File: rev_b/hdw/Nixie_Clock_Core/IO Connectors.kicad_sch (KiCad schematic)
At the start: 4 parts

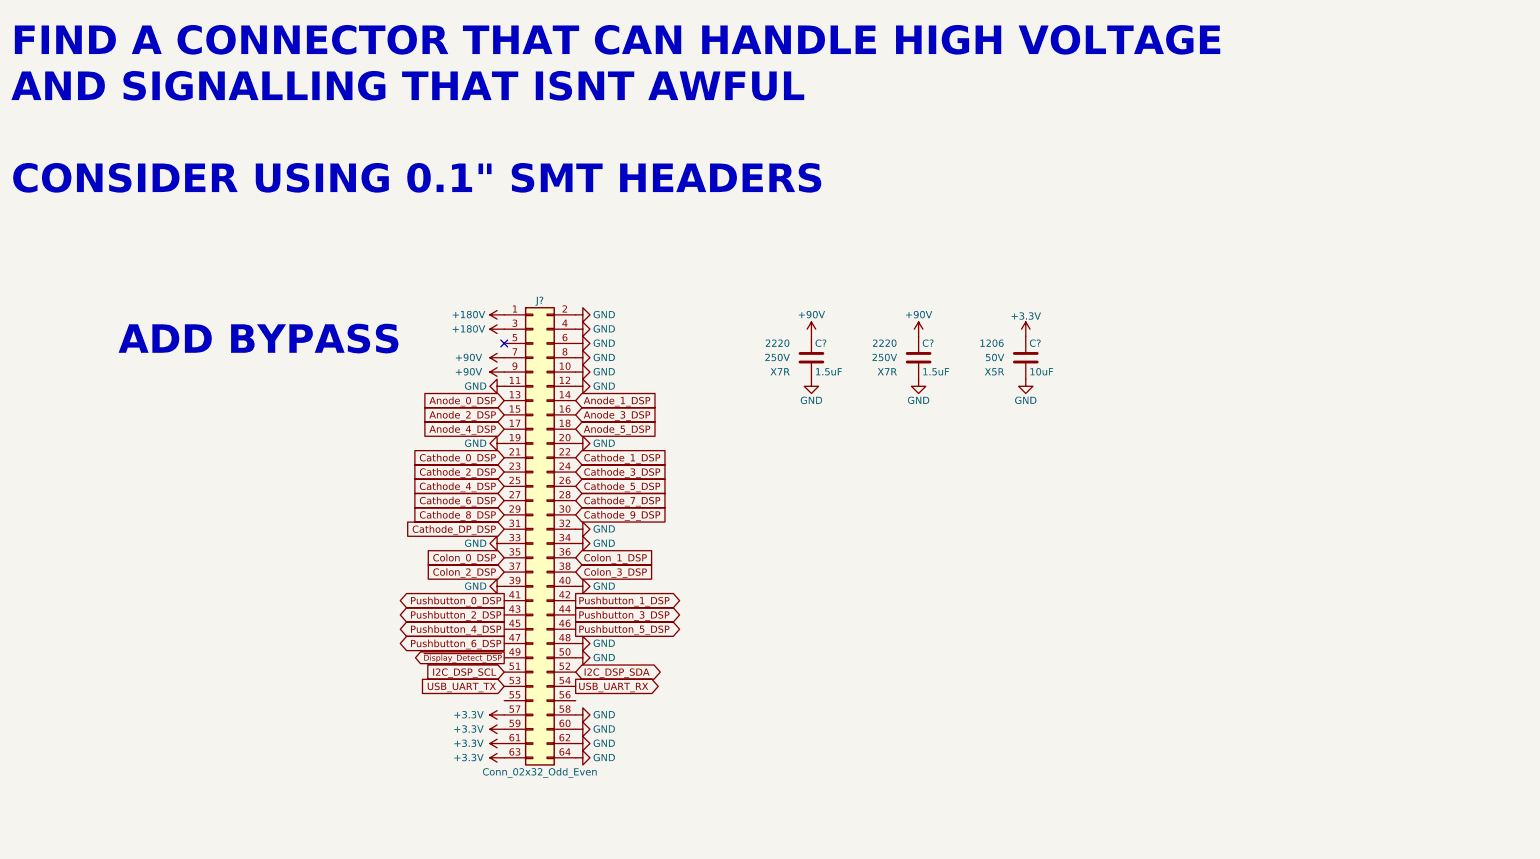
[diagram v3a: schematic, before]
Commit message: updated footprints, ran some DRC
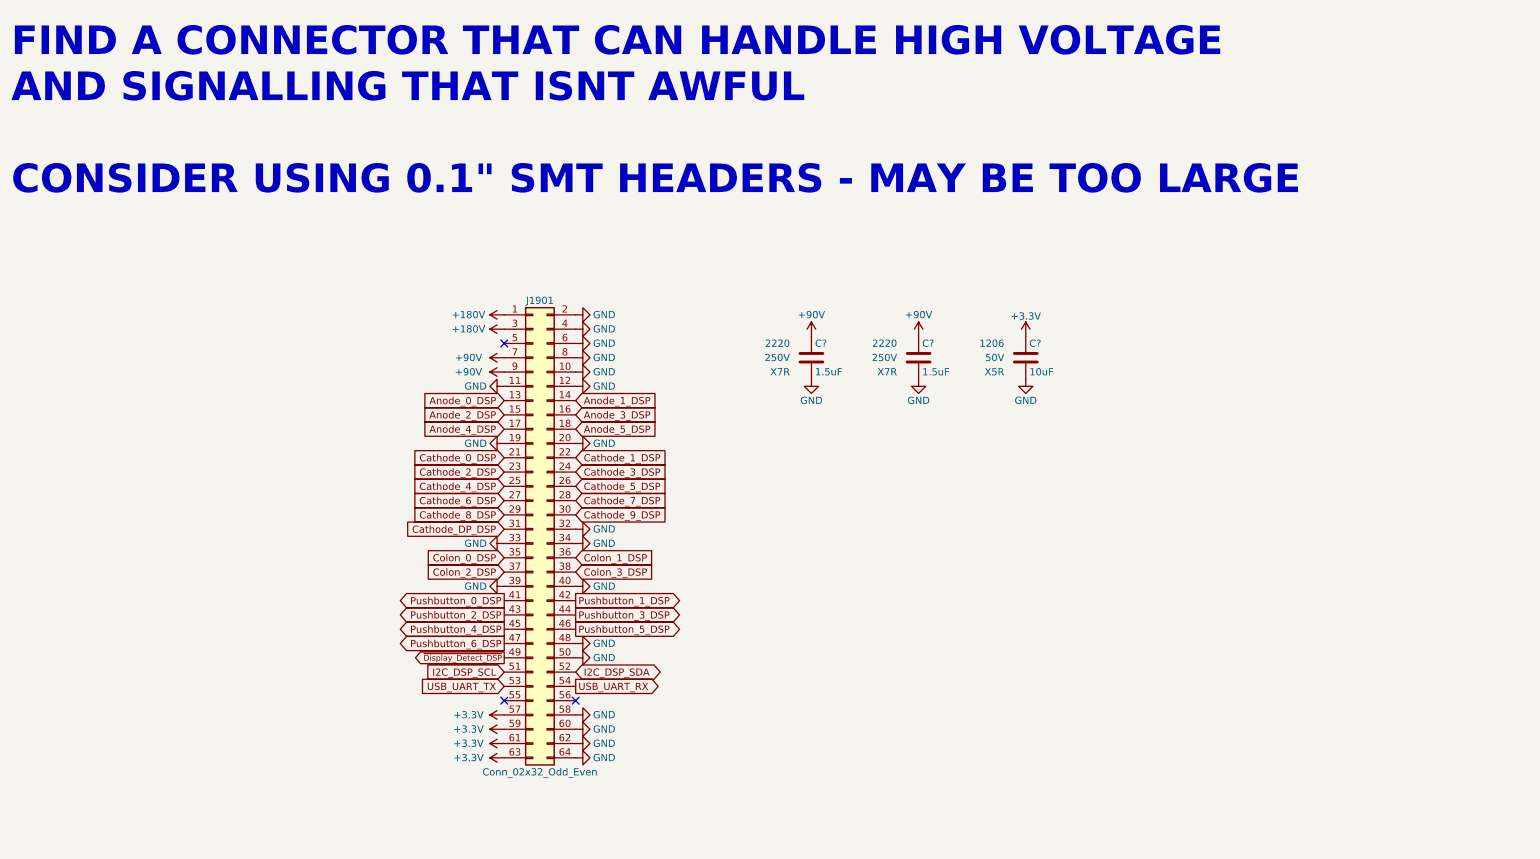
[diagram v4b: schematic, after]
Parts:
- C? (x2): footprint (none) -> Capacitors_SMD:C_2220; Digi-Key PN 565-4697-1-ND -> (none)
- C?: footprint (none) -> Capacitors_SMD:C_1206; Digi-Key PN 1276-6736-1-ND -> (none)
- J1901: renamed from J?; footprint (none) -> Connector_PinSocket_2.54mm:PinSocket_2x32_P2.54mm_Vertical_SMD
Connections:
- no-connect marks 1 -> 3
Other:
- note added: "FIND A CONNECTOR THAT CAN HANDLE HIGH VOLTAGE AND SIGNALLING THAT ISNT AWFUL CONSIDER USING 0.1" SMT HEADERS - MAY BE TOO LARGE"
- note removed: "ADD BYPASS"
- note removed: "FIND A CONNECTOR THAT CAN HANDLE HIGH VOLTAGE AND SIGNALLING THAT ISNT AWFUL CONSIDER USING 0.1" SMT HEADERS"
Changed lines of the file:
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@@
     (company "Drew Maatman")
   )
+  (no_connect (at 137.16 137.795))
+  (no_connect (at 124.46 137.795))
   (no_connect (at 124.46 74.295))
-  (text "ADD BYPASS" (at 55.88 76.835 0)
-    (effects (font (face "Courier New") (size 5.08 5.08) (thickness 0.254) bold (color 255 37 56 1)) (justify left bottom))
-  )
-  (text "FIND A CONNECTOR THAT CAN HANDLE HIGH VOLTAGE\nAND SIGNALLING THAT ISNT AWFUL\n\nCONSIDER USING 0.1\" SMT HEADERS"
+  (text "FIND A CONNECTOR THAT CAN HANDLE HIGH VOLTAGE\nAND SIGNALLING THAT ISNT AWFUL\n\nCONSIDER USING 0.1\" SMT HEADERS - MAY BE TOO LARGE"
     (at 36.83 48.26 0)
     (effects (font (face "Courier New") (size 5.08 5.08) (thickness 0.254) bold (color 255 37 56 1)) (justify left bottom))
@@
       (effects (font (size 1.27 1.27)) (justify left))
     )
-    (property "Footprint" "" (at 199.0852 80.645 0)
+    (property "Footprint" "Capacitors_SMD:C_2220" (at 199.0852 80.645 0)
       (effects (font (size 1.27 1.27)) hide)
     )
@@
       (effects (font (size 1.27 1.27)) (justify right))
     )
-    (property "Digi-Key PN" "565-4697-1-ND" (at 208.915 64.135 0)
+    (property "Digi-Key PN" "" (at 208.915 64.135 0)
       (effects (font (size 1.524 1.524)) hide)
     )
@@
         )
         (path "/16fdce21-b570-4d81-a458-e8839d611806/2e22fd27-425d-47fb-8810-3fe495af3afd"
-          (reference "C?") (unit 1)
+          (reference "C1902") (unit 1)
         )
       )
@@
       (effects (font (size 1.27 1.27)) (justify left))
     )
-    (property "Footprint" "" (at 218.1352 80.645 0)
+    (property "Footprint" "Capacitors_SMD:C_1206" (at 218.1352 80.645 0)
       (effects (font (size 1.27 1.27)) hide)
     )
@@
       (effects (font (size 1.27 1.27)) (justify right))
     )
-    (property "Digi-Key PN" "1276-6736-1-ND" (at 227.965 64.135 0)
+    (property "Digi-Key PN" "" (at 227.965 64.135 0)
       (effects (font (size 1.524 1.524)) hide)
     )
@@
         )
         (path "/16fdce21-b570-4d81-a458-e8839d611806/2e22fd27-425d-47fb-8810-3fe495af3afd"
-          (reference "C?") (unit 1)
+          (reference "C1903") (unit 1)
         )
       )
@@
   (symbol (lib_id "Connector_Generic:Conn_02x32_Odd_Even") (at 129.54 107.315 0) (unit 1)
     (in_bom yes) (on_board yes) (dnp no)
-    (property "Reference" "J?" (at 130.81 66.675 0)
+    (property "Reference" "J1901" (at 130.81 66.675 0)
       (effects (font (size 1.27 1.27)))
     )
@@
       (effects (font (size 1.27 1.27)))
     )
-    (property "Footprint" "" (at 129.54 107.315 0)
+    (property "Footprint" "Connector_PinSocket_2.54mm:PinSocket_2x32_P2.54mm_Vertical_SMD" (at 129.54 107.315 0)
       (effects (font (size 1.27 1.27)) hide)
     )
@@
       (project "Nixie_Clock_Core"
         (path "/16fdce21-b570-4d81-a458-e8839d611806/2e22fd27-425d-47fb-8810-3fe495af3afd"
-          (reference "J?") (unit 1)
+          (reference "J1901") (unit 1)
         )
       )
@@
       (effects (font (size 1.27 1.27)) (justify left))
     )
-    (property "Footprint" "" (at 180.0352 80.645 0)
+    (property "Footprint" "Capacitors_SMD:C_2220" (at 180.0352 80.645 0)
       (effects (font (size 1.27 1.27)) hide)
     )
@@
       (effects (font (size 1.27 1.27)) (justify right))
     )
-    (property "Digi-Key PN" "565-4697-1-ND" (at 189.865 64.135 0)
+    (property "Digi-Key PN" "" (at 189.865 64.135 0)
       (effects (font (size 1.524 1.524)) hide)
     )
@@
         )
         (path "/16fdce21-b570-4d81-a458-e8839d611806/2e22fd27-425d-47fb-8810-3fe495af3afd"
-          (reference "C?") (unit 1)
-        )
-      )
+          (reference "C1901") (unit 1)
+        )
+      )

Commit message: hid all passive refdes on core PCB
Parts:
- C?: Digi-Key PN (none) -> 1276-6767-1-ND
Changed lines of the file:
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@@
       (effects (font (size 1.27 1.27)) (justify right))
     )
-    (property "Digi-Key PN" "" (at 227.965 64.135 0)
+    (property "Digi-Key PN" "1276-6767-1-ND" (at 227.965 64.135 0)
       (effects (font (size 1.524 1.524)) hide)
     )

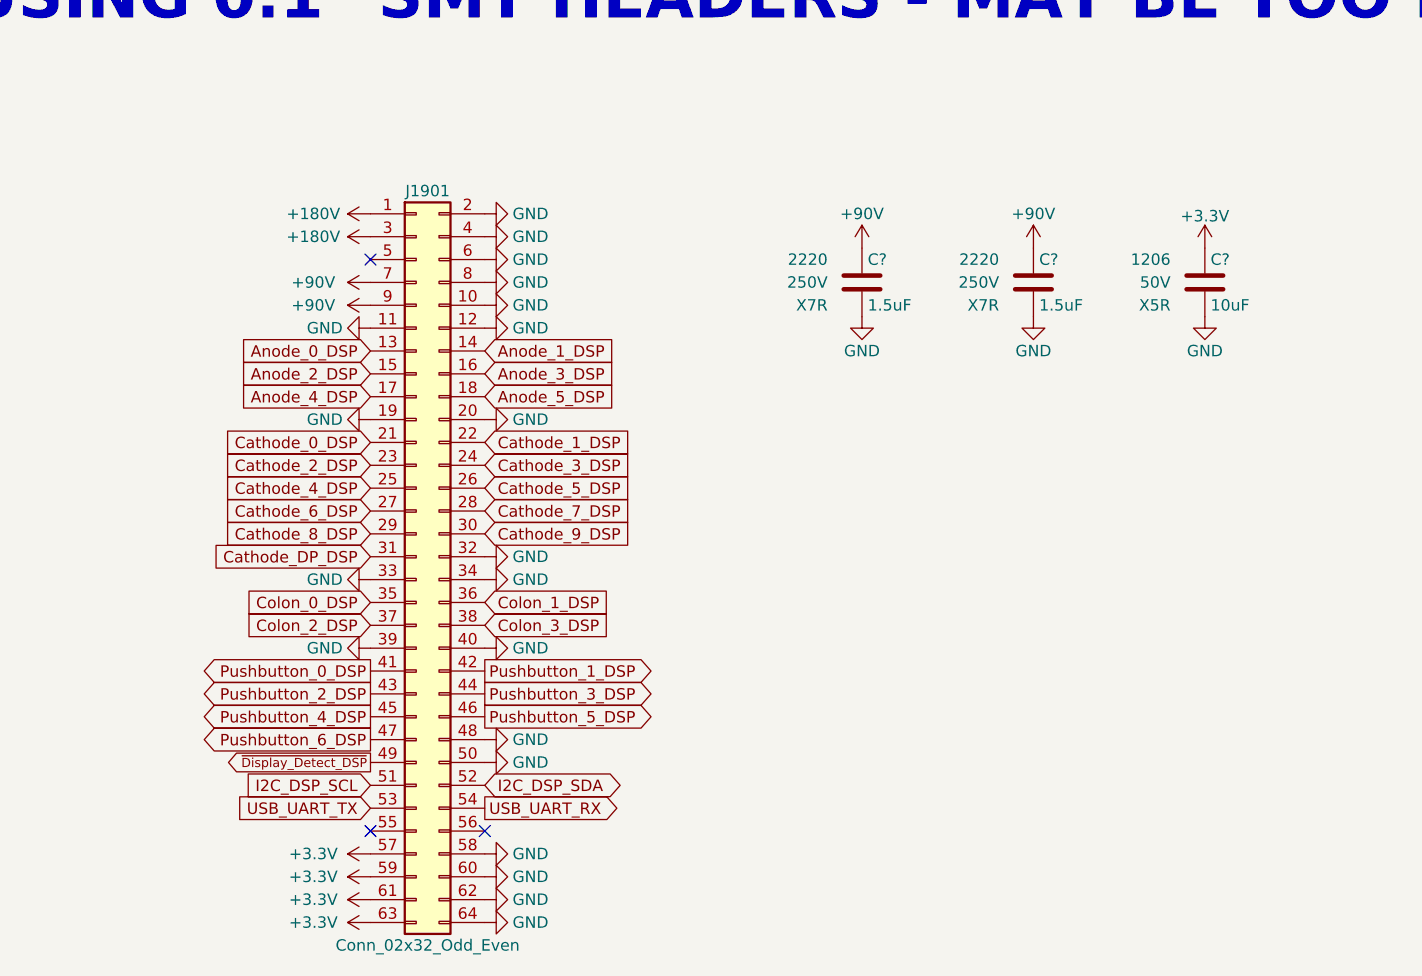
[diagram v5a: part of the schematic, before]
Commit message: chose new IO connector, fixed some net connectivity issues
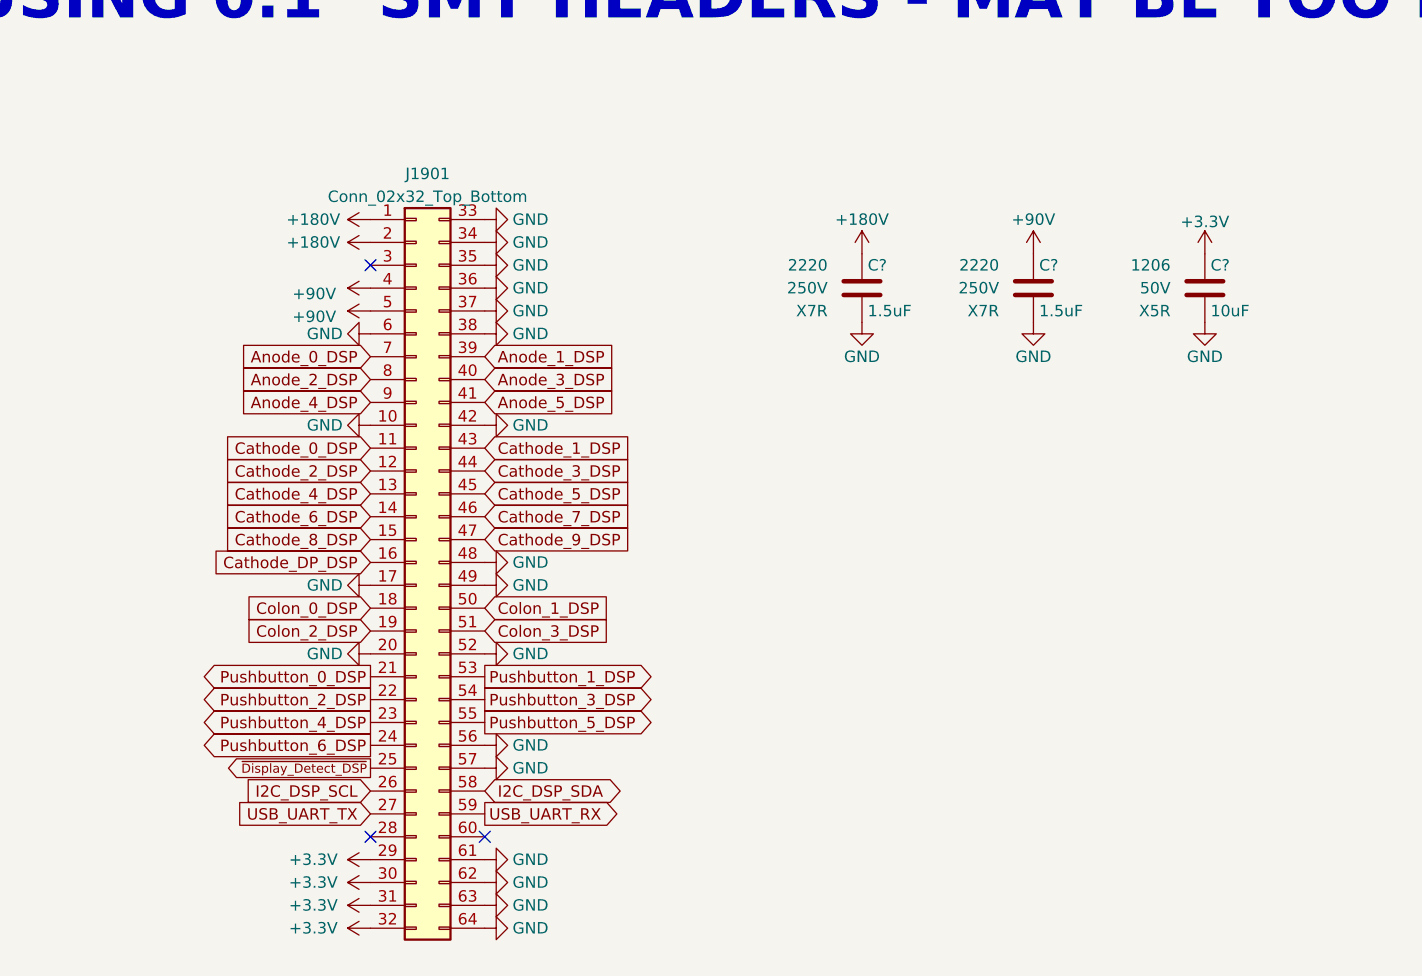
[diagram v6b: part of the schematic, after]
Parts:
- removed J1901: Conn_02x32_Odd_Even, Connector_PinSocket_2.54mm:PinSocket_2x32_P2.54mm_Vertical_SMD, symbol Connector_Generic:Conn_02x32_Odd_Even
- added J1901: Conn_02x32_Top_Bottom, Custom Footprints Library:CONN_5120527-1_TYC, symbol Connector_Generic:Conn_02x32_Top_Bottom
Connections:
- net +180V: now also C?.1, J1901.1 (Pin_1), J1901.2 (Pin_2)
- net +3.3V: now also J1901.29 (Pin_29), J1901.30 (Pin_30), J1901.31 (Pin_31), J1901.32 (Pin_32)
- net +90V: now also J1901.4 (Pin_4), J1901.5 (Pin_5); no longer C?.1
- net Anode_0_DSP: now also J1901.7 (Pin_7)
- net Anode_1_DSP: now also J1901.39 (Pin_39)
- net Anode_2_DSP: now also J1901.8 (Pin_8)
- net Anode_3_DSP: now also J1901.40 (Pin_40)
- net Anode_4_DSP: now also J1901.9 (Pin_9)
- net Anode_5_DSP: now also J1901.41 (Pin_41)
- net Cathode_0_DSP: now also J1901.11 (Pin_11)
- net Cathode_1_DSP: now also J1901.43 (Pin_43)
- net Cathode_2_DSP: now also J1901.12 (Pin_12)
- net Cathode_3_DSP: now also J1901.44 (Pin_44)
- net Cathode_4_DSP: now also J1901.13 (Pin_13)
- net Cathode_5_DSP: now also J1901.45 (Pin_45)
- net Cathode_6_DSP: now also J1901.14 (Pin_14)
- net Cathode_7_DSP: now also J1901.46 (Pin_46)
- net Cathode_8_DSP: now also J1901.15 (Pin_15)
- net Cathode_9_DSP: now also J1901.47 (Pin_47)
- net Cathode_DP_DSP: now also J1901.16 (Pin_16)
- net Colon_0_DSP: now also J1901.18 (Pin_18)
- net Colon_1_DSP: now also J1901.50 (Pin_50)
- net Colon_2_DSP: now also J1901.19 (Pin_19)
- net Colon_3_DSP: now also J1901.51 (Pin_51)
- net GND: now also J1901.10 (Pin_10), J1901.17 (Pin_17), J1901.20 (Pin_20), J1901.33 (Pin_33), J1901.34 (Pin_34), J1901.35 (Pin_35), J1901.36 (Pin_36), J1901.37 (Pin_37), J1901.38 (Pin_38), J1901.42 (Pin_42), J1901.48 (Pin_48), J1901.49 (Pin_49), J1901.52 (Pin_52), J1901.56 (Pin_56), J1901.57 (Pin_57), J1901.6 (Pin_6), J1901.61 (Pin_61), J1901.62 (Pin_62), J1901.63 (Pin_63), J1901.64 (Pin_64)
- net I2C_DSP_SCL: now also J1901.26 (Pin_26)
- net I2C_DSP_SDA: now also J1901.58 (Pin_58)
- net Pushbutton_0_DSP: now also J1901.21 (Pin_21)
- net Pushbutton_1_DSP: now also J1901.53 (Pin_53)
- net Pushbutton_2_DSP: now also J1901.22 (Pin_22)
- net Pushbutton_3_DSP: now also J1901.54 (Pin_54)
- net Pushbutton_4_DSP: now also J1901.23 (Pin_23)
- net Pushbutton_5_DSP: now also J1901.55 (Pin_55)
- net Pushbutton_6_DSP: now also J1901.24 (Pin_24)
- net USB_UART_RX: now also J1901.59 (Pin_59)
- net USB_UART_TX: now also J1901.27 (Pin_27)
- net ~{Display_Detect_DSP}: now also J1901.25 (Pin_25)
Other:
- moved on the sheet: C?

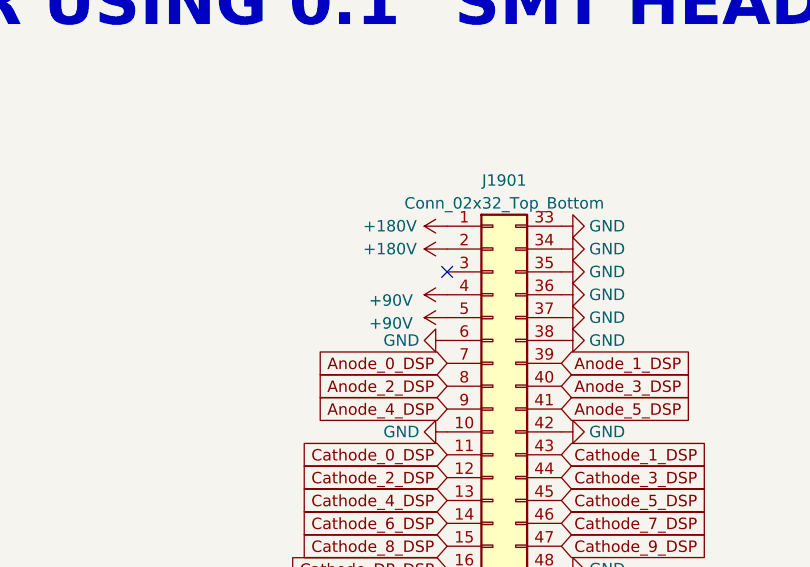
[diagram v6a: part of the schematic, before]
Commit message: lots more core board routing
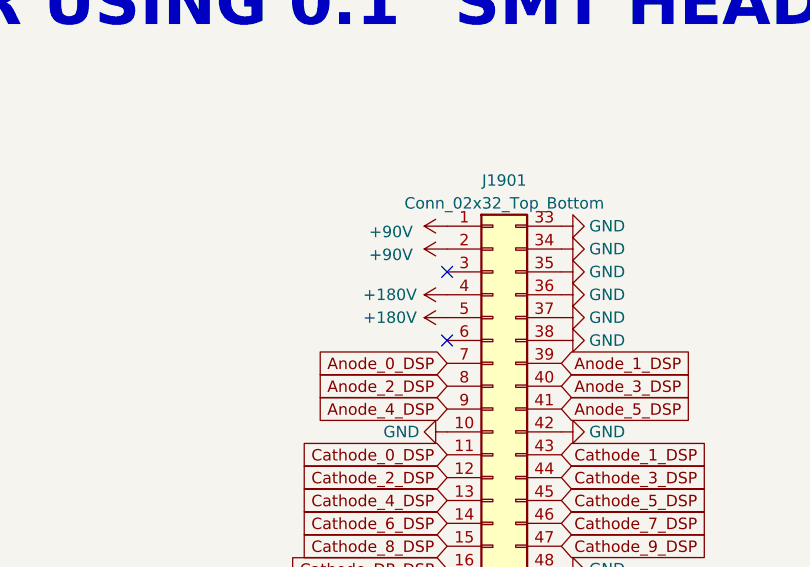
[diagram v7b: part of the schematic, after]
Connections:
- net +180V: now also J1901.4 (Pin_4), J1901.5 (Pin_5); no longer J1901.1 (Pin_1), J1901.2 (Pin_2)
- net +90V: now also J1901.1 (Pin_1), J1901.2 (Pin_2); no longer J1901.4 (Pin_4), J1901.5 (Pin_5)
- net GND: no longer J1901.6 (Pin_6)
- no-connect marks 3 -> 4
